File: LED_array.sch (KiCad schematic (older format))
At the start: 129 parts, among them J1 5040500691

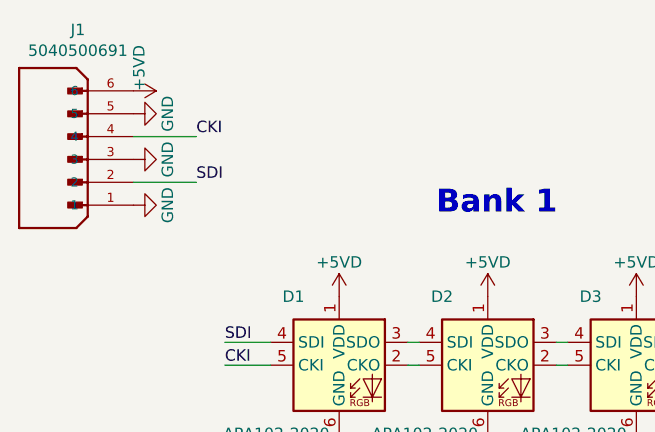
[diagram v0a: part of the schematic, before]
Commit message: Adding in resistors and capacitor pads
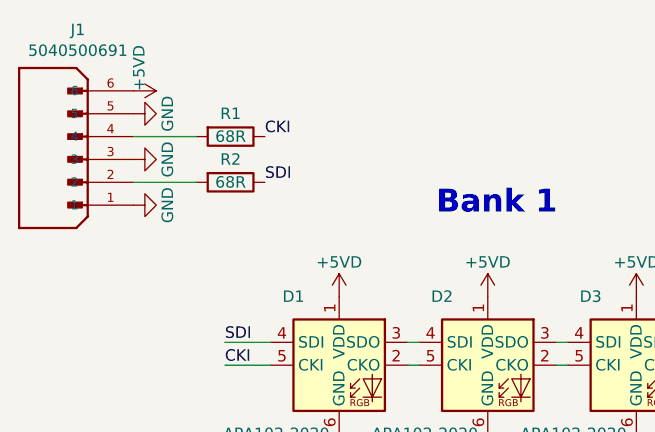
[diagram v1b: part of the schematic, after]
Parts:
- added R1, R2: 68R, Resistor_SMD:R_0603_1608Metric, symbol Device:R
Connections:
- net CKI: now also R1.1; no longer J1.4
- net SDI: now also R2.1; no longer J1.2
- new net: J1.2, R2.2
- new net: J1.4, R1.2
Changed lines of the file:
@@
 	0    -1   -1   0
 $EndComp
-Text Label 1400 1600 0    50   ~ 0
+Text Label 1700 1600 0    50   ~ 0
 CKI
-Text Label 1400 1800 0    50   ~ 0
+Text Label 1700 1800 0    50   ~ 0
 SDI
+$Comp
+L Device:R R1
+U 1 1 606E058F
+P 1550 1600
+F 0 "R1" V 1450 1600 50  0000 C CNN
+F 1 "68R" V 1550 1600 50  0000 C CNN
+F 2 "Resistor_SMD:R_0603_1608Metric" V 1480 1600 50  0001 C CNN
+F 3 "~" H 1550 1600 50  0001 C CNN
+	1    1550 1600
+	0    1    1    0
+$EndComp
+$Comp
+L Device:R R2
+U 1 1 606E627E
+P 1550 1800
+F 0 "R2" V 1450 1800 50  0000 C CNN
+F 1 "68R" V 1550 1800 50  0000 C CNN
+F 2 "Resistor_SMD:R_0603_1608Metric" V 1480 1800 50  0001 C CNN
+F 3 "~" H 1550 1800 50  0001 C CNN
+	1    1550 1800
+	0    1    1    0
+$EndComp
 $EndSCHEMATC

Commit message: minor edits + generation of fab files edits: (1) add capacitors (2) change via and track size for the picolock conenctor (3) update the picolock connector footprint for handsoldering (4) remove label D1-D128 and the 1s (5) change corner to round (6) add text notes for the board
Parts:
- added C1, C2, C3, C4: 4.7u, Capacitor_SMD:C_1206_3216Metric, symbol Device:C
- J1: symbol 5040500691:5040500691 -> LED_array-rescue:5040500691-5040500691
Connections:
- net +5VD: now also C1.1, C2.1, C3.1, C4.1
- net GND: now also C1.2, C2.2, C3.2, C4.2
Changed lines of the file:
@@
 $EndComp
 $Comp
-L 5040500691:5040500691 J1
+L LED_array-rescue:5040500691-5040500691 J1
 U 1 1 605C68B2
 P 925 1600
@@
 	0    1    1    0
 $EndComp
+$Comp
+L Device:C C1
+U 1 1 607A30BD
+P 2350 1200
+F 0 "C1" H 2465 1246 50  0000 L CNN
+F 1 "4.7u" H 2465 1155 50  0000 L CNN
+F 2 "Capacitor_SMD:C_1206_3216Metric" H 2388 1050 50  0001 C CNN
+F 3 "~" H 2350 1200 50  0001 C CNN
+	1    2350 1200
+	1    0    0    -1
+$EndComp
+$Comp
+L Device:C C3
+U 1 1 607A4502
+P 3050 1200
+F 0 "C3" H 3165 1246 50  0000 L CNN
+F 1 "4.7u" H 3165 1155 50  0000 L CNN
+F 2 "Capacitor_SMD:C_1206_3216Metric" H 3088 1050 50  0001 C CNN
+F 3 "~" H 3050 1200 50  0001 C CNN
+	1    3050 1200
+	1    0    0    -1
+$EndComp
+$Comp
+L Device:C C4
+U 1 1 607A4D30
+P 3450 1200
+F 0 "C4" H 3565 1246 50  0000 L CNN
+F 1 "4.7u" H 3565 1155 50  0000 L CNN
+F 2 "Capacitor_SMD:C_1206_3216Metric" H 3488 1050 50  0001 C CNN
+F 3 "~" H 3450 1200 50  0001 C CNN
+	1    3450 1200
+	1    0    0    -1
+$EndComp
+Wire Wire Line
+	2350 1050 2700 1050
+Connection ~ 2700 1050
+Connection ~ 3050 1050
+Wire Wire Line
+	3050 1050 3450 1050
+Wire Wire Line
+	2350 1350 2700 1350
+Connection ~ 2700 1350
+Wire Wire Line
+	2700 1350 2900 1350
+Connection ~ 3050 1350
+Wire Wire Line
+	3050 1350 3450 1350
+$Comp
+L power:GND #PWR0263
+U 1 1 607FAE01
+P 2900 1350
+F 0 "#PWR0263" H 2900 1100 50  0001 C CNN
+F 1 "GND" H 2905 1177 50  0000 C CNN
+F 2 "" H 2900 1350 50  0001 C CNN
+F 3 "" H 2900 1350 50  0001 C CNN
+	1    2900 1350
+	1    0    0    -1
+$EndComp
+Connection ~ 2900 1350
+Wire Wire Line
+	2900 1350 3050 1350
+$Comp
+L Device:C C2
+U 1 1 607A3D5B
+P 2700 1200
+F 0 "C2" H 2815 1246 50  0000 L CNN
+F 1 "4.7u" H 2815 1155 50  0000 L CNN
+F 2 "Capacitor_SMD:C_1206_3216Metric" H 2738 1050 50  0001 C CNN
+F 3 "~" H 2700 1200 50  0001 C CNN
+	1    2700 1200
+	1    0    0    -1
+$EndComp
+Wire Wire Line
+	2700 1050 2900 1050
+$Comp
+L power:+5VD #PWR?
+U 1 1 608D2B09
+P 2900 1050
+F 0 "#PWR?" H 2900 900 50  0001 C CNN
+F 1 "+5VD" H 2900 1200 50  0000 C CNN
+F 2 "" H 2900 1050 50  0001 C CNN
+F 3 "" H 2900 1050 50  0001 C CNN
+	1    2900 1050
+	1    0    0    -1
+$EndComp
+Connection ~ 2900 1050
+Wire Wire Line
+	2900 1050 3050 1050
 $EndSCHEMATC

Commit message: v2 - add a USB-C connector
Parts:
- added H1, H2, H3: MountingHole, MountingHole:MountingHole_2mm, symbol Mechanical:MountingHole
- added J2: USB4055-30-A, Connector:GCT_USB4055-30-A, symbol Connector:USB4055-30-A
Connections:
- net +5VD: now also J2.A4 (VBUS1.1), J2.A9 (VBUS1.2), J2.B4 (VBUS2.1), J2.B9 (VBUS2.2)
- net GND: now also J2.A1 (GND1.1), J2.A12 (GND1.2), J2.B1 (GND2.1), J2.B12 (GND2.2), J2.S1 (SHIELD), J2.S2 (SHIELD), J2.S3 (SHIELD), J2.S4 (SHIELD)
- net sdi: now reaches J1.2, R2.2
- net sdi: now also J2.A7 (DN1), J2.B7 (DN2)
- net cki: now reaches J1.4, R1.2
- net cki: now also J2.A6 (DP1), J2.B6 (DP2)
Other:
- moved on the sheet: R1, R2
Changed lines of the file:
@@
 	0    -1   -1   0
 $EndComp
-Wire Wire Line
-	1125 1600 1400 1600
-Wire Wire Line
-	1125 1800 1400 1800
 $Comp
 L power:GND #PWR0261
@@
 	0    -1   -1   0
 $EndComp
-Text Label 1700 1600 0    50   ~ 0
+Text Label 2200 1600 0    50   ~ 0
 CKI
-Text Label 1700 1800 0    50   ~ 0
+Text Label 2200 1800 0    50   ~ 0
 SDI
 $Comp
 L Device:R R1
 U 1 1 606E058F
-P 1550 1600
-F 0 "R1" V 1450 1600 50  0000 C CNN
-F 1 "68R" V 1550 1600 50  0000 C CNN
-F 2 "Resistor_SMD:R_0603_1608Metric" V 1480 1600 50  0001 C CNN
-F 3 "~" H 1550 1600 50  0001 C CNN
-	1    1550 1600
+P 2050 1600
+F 0 "R1" V 1950 1600 50  0000 C CNN
+F 1 "68R" V 2050 1600 50  0000 C CNN
+F 2 "Resistor_SMD:R_0603_1608Metric" V 1980 1600 50  0001 C CNN
+F 3 "~" H 2050 1600 50  0001 C CNN
+	1    2050 1600
 	0    1    1    0
 $EndComp
@@
 L Device:R R2
 U 1 1 606E627E
-P 1550 1800
-F 0 "R2" V 1450 1800 50  0000 C CNN
-F 1 "68R" V 1550 1800 50  0000 C CNN
-F 2 "Resistor_SMD:R_0603_1608Metric" V 1480 1800 50  0001 C CNN
-F 3 "~" H 1550 1800 50  0001 C CNN
-	1    1550 1800
+P 2050 1800
+F 0 "R2" V 1950 1800 50  0000 C CNN
+F 1 "68R" V 2050 1800 50  0000 C CNN
+F 2 "Resistor_SMD:R_0603_1608Metric" V 1980 1800 50  0001 C CNN
+F 3 "~" H 2050 1800 50  0001 C CNN
+	1    2050 1800
 	0    1    1    0
 $EndComp
@@
 	2700 1050 2900 1050
 $Comp
-L power:+5VD #PWR?
+L power:+5VD #PWR0264
 U 1 1 608D2B09
 P 2900 1050
-F 0 "#PWR?" H 2900 900 50  0001 C CNN
+F 0 "#PWR0264" H 2900 900 50  0001 C CNN
 F 1 "+5VD" H 2900 1200 50  0000 C CNN
 F 2 "" H 2900 1050 50  0001 C CNN
@@
 Wire Wire Line
 	2900 1050 3050 1050
+$Comp
+L Connector:USB4055-30-A J2
+U 1 1 622E257B
+P 7150 16300
+F 0 "J2" H 7480 16346 50  0000 L CNN
+F 1 "USB4055-30-A" H 7480 16255 50  0000 L CNN
+F 2 "Connector:GCT_USB4055-30-A" H 7150 16300 50  0001 L BNN
+F 3 "" H 7150 16300 50  0001 L BNN
+F 4 "https://www.digikey.com.ua/product-detail/en/gct/USB4055-30-A/2073-USB4055-30-ACT-ND/9859729?utm_source=snapeda&utm_medium=aggregator&utm_campaign=symbol" H 7150 16300 50  0001 L BNN "DIGI-KEY_PURCHASE_URL"
+F 5 "B" H 7150 16300 50  0001 L BNN "PARTREV"
+F 6 "USB4055-30-A" H 7150 16300 50  0001 L BNN "MP"
+F 7 "Manufacturer Recommendations" H 7150 16300 50  0001 L BNN "STANDARD"
+F 8 "USB Type C Receptacle Horizontal Hybrid PCB Top Mount 10 mm Body" H 7150 16300 50  0001 L BNN "DESCRIPTION"
+F 9 "None" H 7150 16300 50  0001 L BNN "PACKAGE"
+F 10 "Global Connector Technology" H 7150 16300 50  0001 L BNN "MANUFACTURER"
+F 11 "2073-USB4055-30-ACT-ND" H 7150 16300 50  0001 L BNN "DIGI-KEY_PART_NUMBER"
+	1    7150 16300
+	1    0    0    -1
+$EndComp
+$Comp
+L power:GND #PWR0265
+U 1 1 6236F915
+P 6350 16100
+F 0 "#PWR0265" H 6350 15850 50  0001 C CNN
+F 1 "GND" H 6355 15927 50  0000 C CNN
+F 2 "" H 6350 16100 50  0001 C CNN
+F 3 "" H 6350 16100 50  0001 C CNN
+	1    6350 16100
+	0    1    1    0
+$EndComp
+$Comp
+L power:GND #PWR0266
+U 1 1 6239CBC4
+P 6350 15000
+F 0 "#PWR0266" H 6350 14750 50  0001 C CNN
+F 1 "GND" H 6355 14827 50  0000 C CNN
+F 2 "" H 6350 15000 50  0001 C CNN
+F 3 "" H 6350 15000 50  0001 C CNN
+	1    6350 15000
+	0    1    1    0
+$EndComp
+$Comp
+L power:GND #PWR0267
+U 1 1 623CA76C
+P 6400 17400
+F 0 "#PWR0267" H 6400 17150 50  0001 C CNN
+F 1 "GND" H 6405 17227 50  0000 C CNN
+F 2 "" H 6400 17400 50  0001 C CNN
+F 3 "" H 6400 17400 50  0001 C CNN
+	1    6400 17400
+	0    1    1    0
+$EndComp
+$Comp
+L power:GND #PWR0268
+U 1 1 623F704D
+P 6350 16300
+F 0 "#PWR0268" H 6350 16050 50  0001 C CNN
+F 1 "GND" H 6355 16127 50  0000 C CNN
+F 2 "" H 6350 16300 50  0001 C CNN
+F 3 "" H 6350 16300 50  0001 C CNN
+	1    6350 16300
+	0    1    1    0
+$EndComp
+Wire Wire Line
+	6650 15000 6350 15000
+Wire Wire Line
+	6350 16100 6650 16100
+Wire Wire Line
+	6350 16300 6650 16300
+Wire Wire Line
+	6400 17400 6650 17400
+$Comp
+L power:+5VD #PWR0269
+U 1 1 6257BD67
+P 6550 15300
+F 0 "#PWR0269" H 6550 15150 50  0001 C CNN
+F 1 "+5VD" V 6565 15428 50  0000 L CNN
+F 2 "" H 6550 15300 50  0001 C CNN
+F 3 "" H 6550 15300 50  0001 C CNN
+	1    6550 15300
+	0    -1   -1   0
+$EndComp
+$Comp
+L power:+5VD #PWR0270
+U 1 1 625DF2A4
+P 6550 15800
+F 0 "#PWR0270" H 6550 15650 50  0001 C CNN
+F 1 "+5VD" V 6565 15928 50  0000 L CNN
+F 2 "" H 6550 15800 50  0001 C CNN
+F 3 "" H 6550 15800 50  0001 C CNN
+	1    6550 15800
+	0    -1   -1   0
+$EndComp
+$Comp
+L power:+5VD #PWR0271
+U 1 1 6260F618
+P 6550 16600
+F 0 "#PWR0271" H 6550 16450 50  0001 C CNN
+F 1 "+5VD" V 6565 16728 50  0000 L CNN
+F 2 "" H 6550 16600 50  0001 C CNN
+F 3 "" H 6550 16600 50  0001 C CNN
+	1    6550 16600
+	0    -1   -1   0
+$EndComp
+$Comp
+L power:+5VD #PWR0272
+U 1 1 6263CCA0
+P 6550 17100
+F 0 "#PWR0272" H 6550 16950 50  0001 C CNN
+F 1 "+5VD" V 6565 17228 50  0000 L CNN
+F 2 "" H 6550 17100 50  0001 C CNN
+F 3 "" H 6550 17100 50  0001 C CNN
+	1    6550 17100
+	0    -1   -1   0
+$EndComp
+Wire Wire Line
+	6550 17100 6650 17100
+Wire Wire Line
+	6550 16600 6650 16600
+Wire Wire Line
+	6550 15800 6650 15800
+Wire Wire Line
+	6550 15300 6650 15300
+Text Label 6350 15500 0    100  ~ 0
+cki
+Text Label 6350 16800 0    100  ~ 0
+cki
+Text Label 6350 15600 0    100  ~ 0
+sdi
+Text Label 6600 16900 2    100  ~ 0
+sdi
+Wire Wire Line
+	6600 16900 6650 16900
+Wire Wire Line
+	6650 16800 6350 16800
+Wire Wire Line
+	6350 15500 6650 15500
+Wire Wire Line
+	6350 15600 6650 15600
+Wire Wire Line
+	1125 1800 1900 1800
+Wire Wire Line
+	1125 1600 1900 1600
+Text Label 1650 1600 0    100  ~ 0
+cki
+Text Label 1650 1800 0    100  ~ 0
+sdi
+$Comp
+L power:GND #PWR0273
+U 1 1 623EFFB0
+P 6650 17600
+F 0 "#PWR0273" H 6650 17350 50  0001 C CNN
+F 1 "GND" H 6655 17427 50  0000 C CNN
+F 2 "" H 6650 17600 50  0001 C CNN
+F 3 "" H 6650 17600 50  0001 C CNN
+	1    6650 17600
+	0    1    1    0
+$EndComp
+$Comp
+L Mechanical:MountingHole H1
+U 1 1 6227506A
+P 10400 15100
+F 0 "H1" H 10500 15146 50  0000 L CNN
+F 1 "MountingHole" H 10500 15055 50  0000 L CNN
+F 2 "MountingHole:MountingHole_2mm" H 10400 15100 50  0001 C CNN
+F 3 "~" H 10400 15100 50  0001 C CNN
+	1    10400 15100
+	1    0    0    -1
+$EndComp
+$Comp
+L Mechanical:MountingHole H2
+U 1 1 6227578F
+P 10400 15450
+F 0 "H2" H 10500 15496 50  0000 L CNN
+F 1 "MountingHole" H 10500 15405 50  0000 L CNN
+F 2 "MountingHole:MountingHole_2mm" H 10400 15450 50  0001 C CNN
+F 3 "~" H 10400 15450 50  0001 C CNN
+	1    10400 15450
+	1    0    0    -1
+$EndComp
+$Comp
+L Mechanical:MountingHole H3
+U 1 1 622758BD
+P 10400 15750
+F 0 "H3" H 10500 15796 50  0000 L CNN
+F 1 "MountingHole" H 10500 15705 50  0000 L CNN
+F 2 "MountingHole:MountingHole_2mm" H 10400 15750 50  0001 C CNN
+F 3 "~" H 10400 15750 50  0001 C CNN
+	1    10400 15750
+	1    0    0    -1
+$EndComp
 $EndSCHEMATC
